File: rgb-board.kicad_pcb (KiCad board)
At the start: 2 copper layers, 178 x 129.5 mm, 89 parts, among them J1 Conn_02x25_Odd_Even, J10 Conn_Coaxial, J11 Conn_Coaxial, J2 SCART-F, J3 TEST_1P, J4 TEST_1P, J5 Conn_Coaxial, J6 Conn_Coaxial, J7 Conn_Coaxial, J8 Conn_Coaxial, J9 Conn_Coaxial, Q101 BC850C, Q105 BC850C, Q109 BC850C, Q113 BC850C, Q114 BC850C, Q201 BC850C, SW1 SW_DPDT_x2, U1 NCP1117-12_SOT223

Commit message: Update project to KiCad 8.
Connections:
- net /B/B-Y renamed /B/B-Y
- net /G/Y renamed /G/Y
- net /HD/CS renamed /HD/CS
- net /R/R-Y renamed /R/R-Y
- J1 pad 10: (no net) -> unconnected-(J1-Pin_10-Pad10)
- J1 pad 15: (no net) -> unconnected-(J1-Pin_15-Pad15)
- J1 pad 16: (no net) -> unconnected-(J1-Pin_16-Pad16)
- J1 pad 17: (no net) -> unconnected-(J1-Pin_17-Pad17)
- J1 pad 18: (no net) -> unconnected-(J1-Pin_18-Pad18)
- J1 pad 20: (no net) -> unconnected-(J1-Pin_20-Pad20)
- J1 pad 22: (no net) -> unconnected-(J1-Pin_22-Pad22)
- J1 pad 23: (no net) -> unconnected-(J1-Pin_23-Pad23)
- J1 pad 24: (no net) -> unconnected-(J1-Pin_24-Pad24)
- J1 pad 26: (no net) -> unconnected-(J1-Pin_26-Pad26)
- J1 pad 27: (no net) -> unconnected-(J1-Pin_27-Pad27)
- J1 pad 28: (no net) -> unconnected-(J1-Pin_28-Pad28)
- J1 pad 29: (no net) -> unconnected-(J1-Pin_29-Pad29)
- J1 pad 30: (no net) -> unconnected-(J1-Pin_30-Pad30)
- J1 pad 32: (no net) -> unconnected-(J1-Pin_32-Pad32)
- J1 pad 33: (no net) -> unconnected-(J1-Pin_33-Pad33)
- J1 pad 34: (no net) -> unconnected-(J1-Pin_34-Pad34)
- J1 pad 35: (no net) -> unconnected-(J1-Pin_35-Pad35)
- J1 pad 36: (no net) -> unconnected-(J1-Pin_36-Pad36)
- J1 pad 37: (no net) -> unconnected-(J1-Pin_37-Pad37)
- J1 pad 38: (no net) -> unconnected-(J1-Pin_38-Pad38)
- J1 pad 40: (no net) -> unconnected-(J1-Pin_40-Pad40)
- J1 pad 42: (no net) -> unconnected-(J1-Pin_42-Pad42)
- J1 pad 43: (no net) -> unconnected-(J1-Pin_43-Pad43)
- J1 pad 44: (no net) -> unconnected-(J1-Pin_44-Pad44)
- J1 pad 45: (no net) -> unconnected-(J1-Pin_45-Pad45)
- J1 pad 46: (no net) -> unconnected-(J1-Pin_46-Pad46)
- J1 pad 8: (no net) -> unconnected-(J1-Pin_8-Pad8)
- J1 pad 9: (no net) -> unconnected-(J1-Pin_9-Pad9)
- J2 pad 1: (no net) -> unconnected-(J2-P1-Pad1)
- J2 pad 10: (no net) -> unconnected-(J2-P10-Pad10)
- J2 pad 12: (no net) -> unconnected-(J2-P12-Pad12)
- J2 pad 14: (no net) -> unconnected-(J2-P14-Pad14)
- J2 pad 16: (no net) -> unconnected-(J2-P16-Pad16)
- J2 pad 19: (no net) -> unconnected-(J2-P19-Pad19)
- J2 pad 3: (no net) -> unconnected-(J2-P3-Pad3)
- J2 pad 8: (no net) -> unconnected-(J2-P8-Pad8)
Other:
- net class Default removed

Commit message: Remove BNC connectors.
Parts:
- removed J5, J6, J7, J8, J9: Conn_Coaxial, bnc-tht:BNC-THT

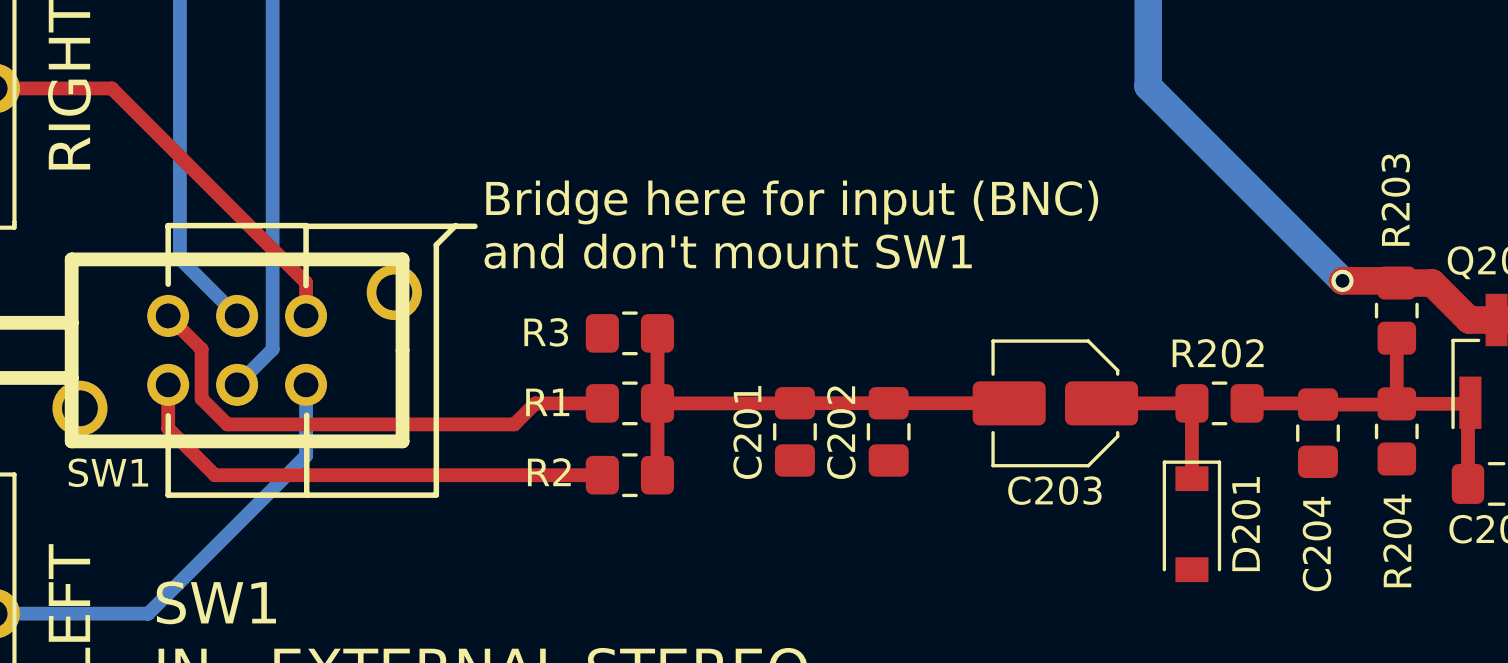
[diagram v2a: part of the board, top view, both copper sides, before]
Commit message: Remove BNC connectors.
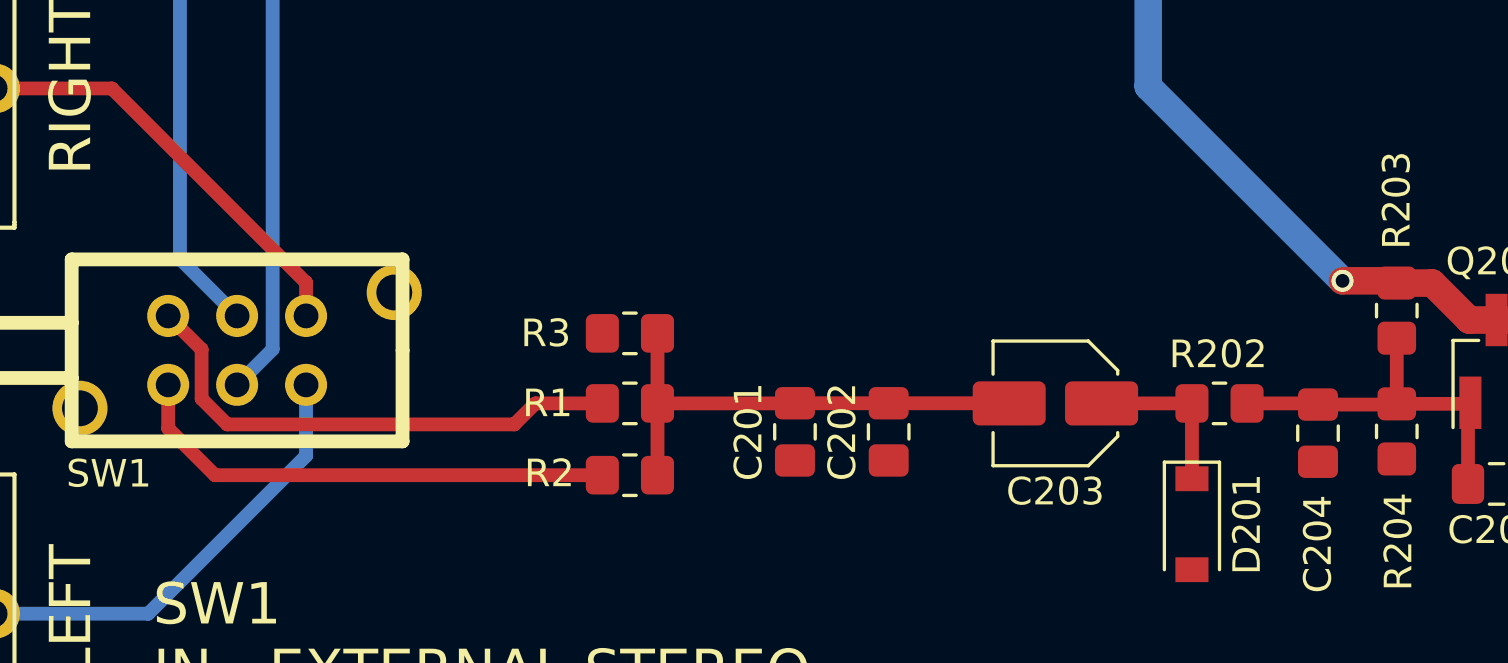
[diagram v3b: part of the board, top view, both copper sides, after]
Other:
- board text removed: "Bridge here for input (BNC) and don't mount SW1"
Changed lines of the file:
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@@
-	)
-	(gr_line
-		(start 65.55 137.6)
-		(end 65.55 135.525)
-		(stroke
-			(width 0.2)
-			(type solid)
-		)
-		(layer "F.SilkS")
 	)
 	(gr_line
@@
 	)
 	(gr_line
-		(start 70.575 142.35)
-		(end 70.575 145.25)
-		(stroke
-			(width 0.2)
-			(type solid)
-		)
-		(layer "F.SilkS")
-	)
-	(gr_line
-		(start 75.275 136.175)
-		(end 75.975 135.475)
-		(stroke
-			(width 0.2)
-			(type solid)
-		)
-		(layer "F.SilkS")
-	)
-	(gr_line
-		(start 65.55 135.475)
-		(end 65.55 135.525)
-		(stroke
-			(width 0.2)
-			(type solid)
-		)
-		(layer "F.SilkS")
-	)
-	(gr_line
 		(start 106.68 121.92)
 		(end 71.12 121.92)
@@
 	)
 	(gr_line
-		(start 70.55 135.475)
-		(end 65.55 135.475)
-		(stroke
-			(width 0.2)
-			(type solid)
-		)
-		(layer "F.SilkS")
-	)
-	(gr_line
-		(start 75.275 145.225)
-		(end 75.275 136.175)
-		(stroke
-			(width 0.2)
-			(type solid)
-		)
-		(layer "F.SilkS")
-	)
-	(gr_line
-		(start 65.55 142.375)
-		(end 65.55 145.25)
-		(stroke
-			(width 0.2)
-			(type solid)
-		)
-		(layer "F.SilkS")
-	)
-	(gr_line
-		(start 70.55 135.5)
-		(end 76.675 135.5)
-		(stroke
-			(width 0.2)
-			(type solid)
-		)
-		(layer "F.SilkS")
-	)
-	(gr_line
-		(start 70.55 137.65)
-		(end 70.55 135.475)
-		(stroke
-			(width 0.2)
-			(type solid)
-		)
-		(layer "F.SilkS")
-	)
-	(gr_line
 		(start 236.5 127.4)
 		(end 236.5 127.375)
@@
 	)
 	(gr_line
-		(start 65.55 145.25)
-		(end 75.275 145.25)
-		(stroke
-			(width 0.2)
-			(type solid)
-		)
-		(layer "F.SilkS")
-	)
-	(gr_line
 		(start 56.8 93.7)
 		(end 60.15 93.7)
@@
 		)
 	)
-	(gr_text "Bridge here for input (BNC)\nand don't mount SW1"
-		(at 76.925 135.5 0)
-		(layer "F.SilkS")
-		(effects
-			(font
-				(size 1.2 1.2)
-				(thickness 0.25)
-			)
-			(justify left)
-		)
-	)

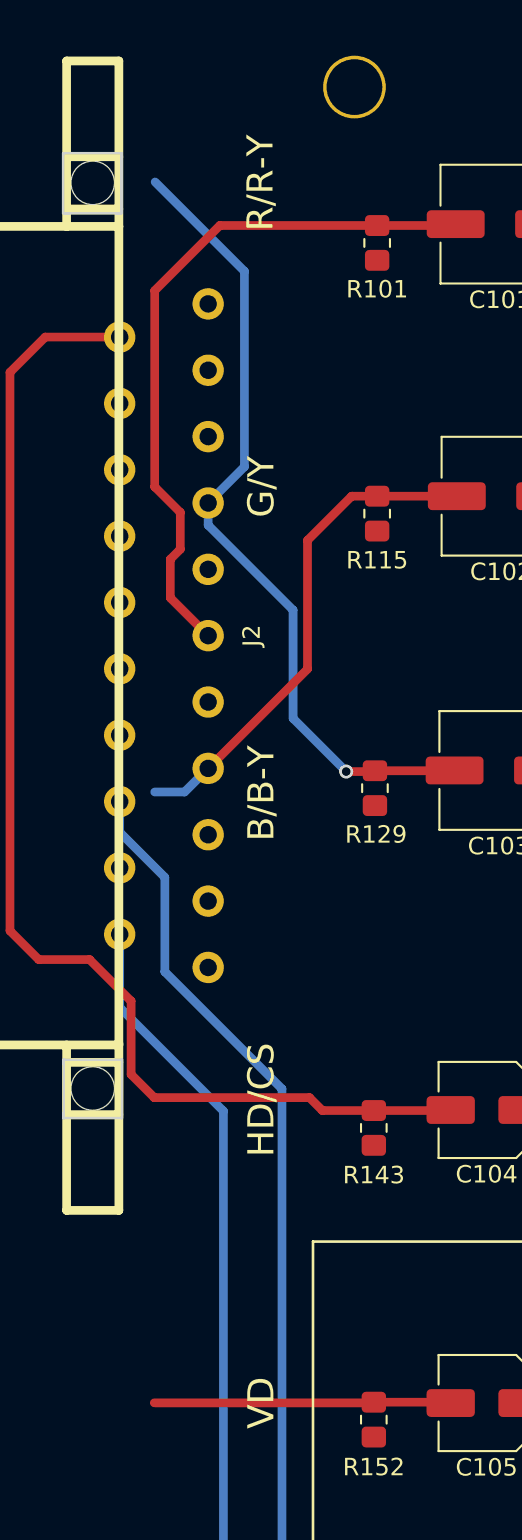
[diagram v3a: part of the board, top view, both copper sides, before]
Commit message: Remove BNC connectors.
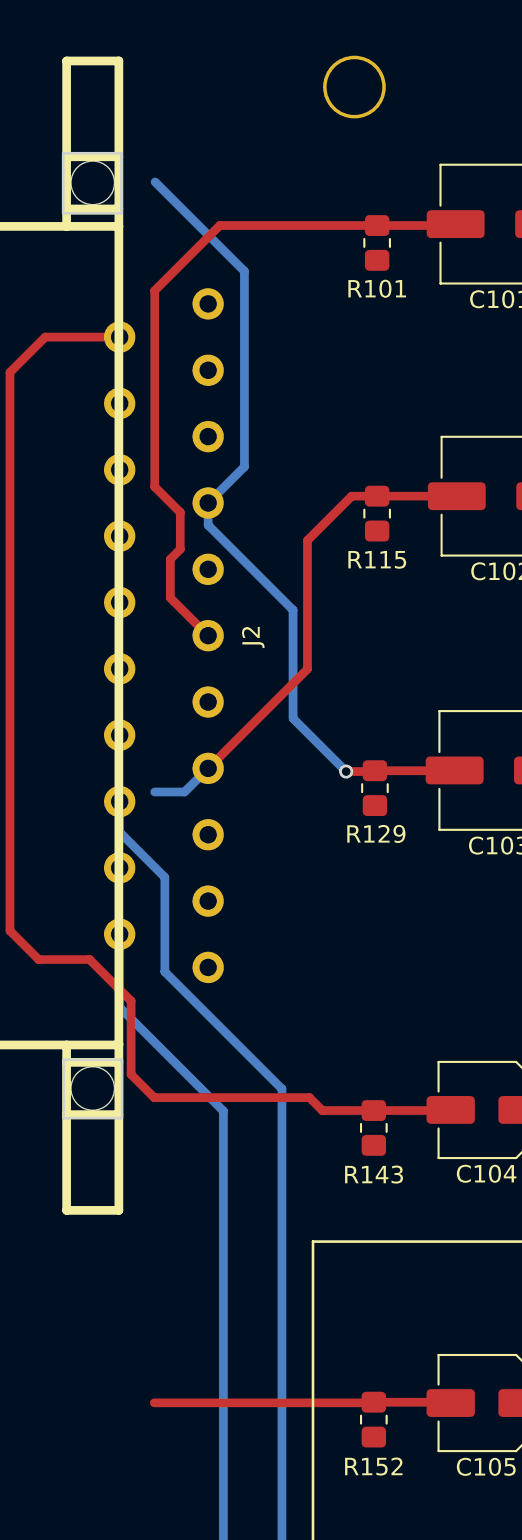
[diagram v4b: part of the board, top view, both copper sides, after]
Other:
- board text removed: "B/B-Y"
- board text removed: "G/Y"
- board text removed: "HD/CS"
- board text removed: "R/R-Y"
- board text removed: "VD"
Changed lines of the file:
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@@
-		)
-	)
-	(gr_text "VD"
-		(at 68.15 113.4 90)
-		(layer "F.SilkS")
-		(effects
-			(font
-				(size 1.5 1.5)
-				(thickness 0.3)
-			)
 		)
 	)
 	(gr_text "JVC IF-C01COMG (RGB/YPbPr) SCART/BNC SMD CLONE BOARD\n(2021) Martin Hejnfelt (martin@hejnfelt.com)\n\nDual input idea credit goes to James Vanderloeff!\n"
 		(at 182.45 39.675 0)
-		(layer "F.SilkS")
-		(effects
-			(font
-				(size 1.5 1.5)
-				(thickness 0.3)
-			)
-		)
-	)
-	(gr_text "R/R-Y"
-		(at 68.1 43.35 90)
 		(layer "F.SilkS")
 		(effects
@@
 		)
 	)
-	(gr_text "G/Y"
-		(at 68.15 60.8 90)
-		(layer "F.SilkS")
-		(effects
-			(font
-				(size 1.5 1.5)
-				(thickness 0.3)
-			)
-		)
-	)
-	(gr_text "B/B-Y"
-		(at 68.15 78.4 90)
-		(layer "F.SilkS")
-		(effects
-			(font
-				(size 1.5 1.5)
-				(thickness 0.3)
-			)
-		)
-	)
 	(gr_text "Do NOT mount\nthis section\nwhen using SCART"
 		(at 110.49 112.9665 90)
@@
 			)
 		)
-	)
-	(gr_text "HD/CS"
-		(at 68.15 96 90)
-		(layer "F.SilkS")
-		(effects
-			(font
-				(size 1.5 1.5)
-				(thickness 0.3)
-			)
-		)

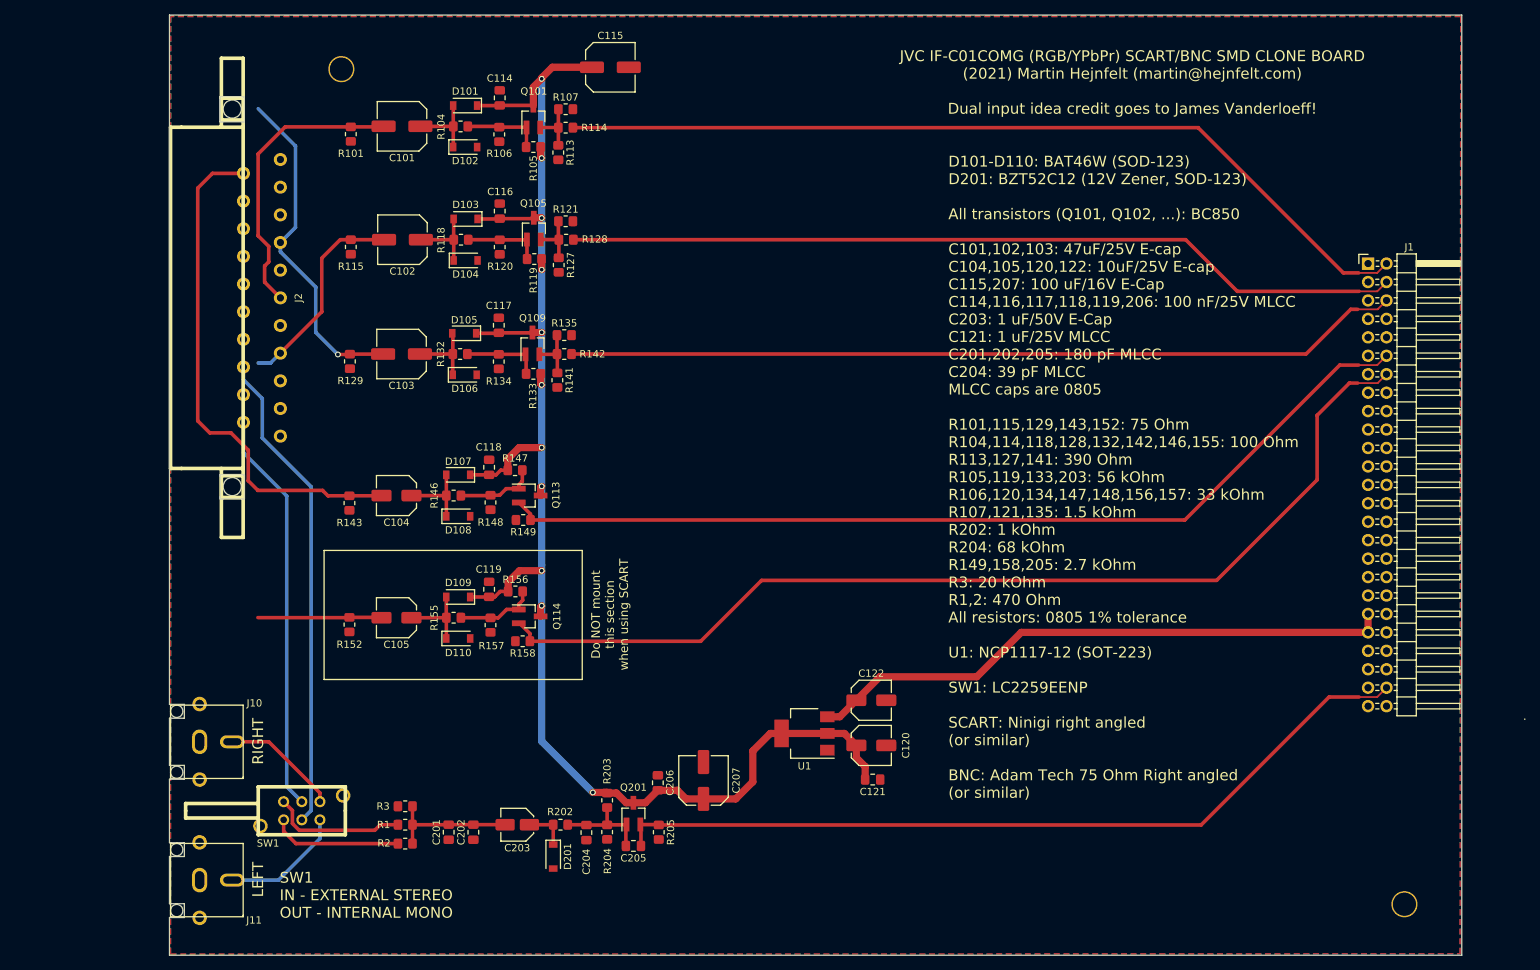
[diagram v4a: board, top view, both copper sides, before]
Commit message: Remove BNC connectors.
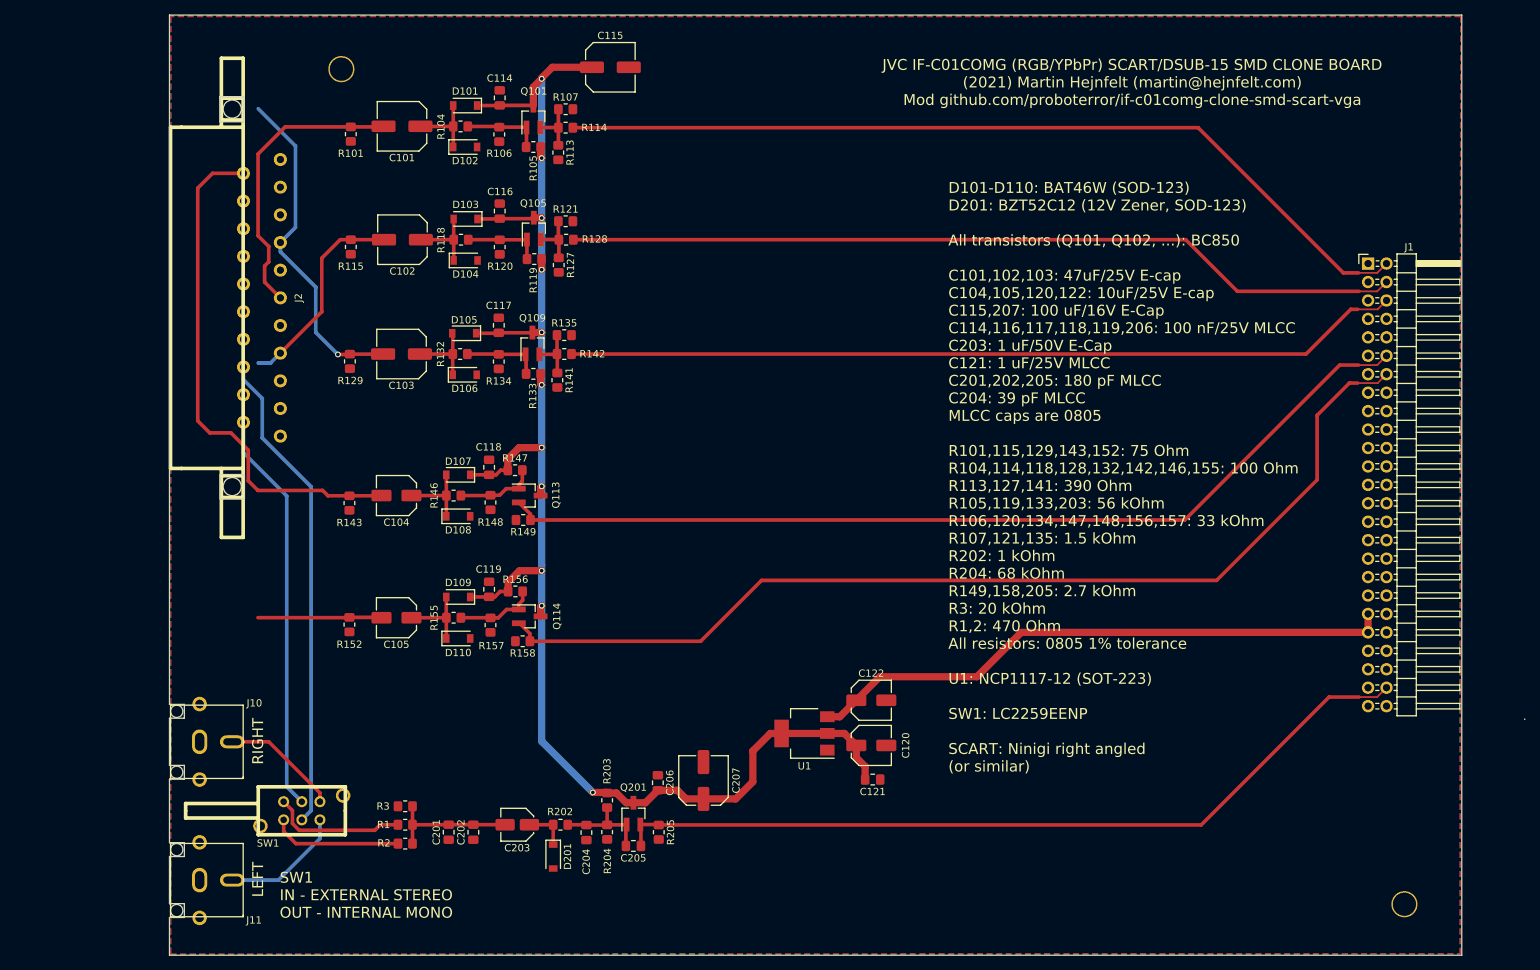
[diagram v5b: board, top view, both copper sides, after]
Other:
- board text added: "JVC IF-C01COMG (RGB/YPbPr) SCART/DSUB-15 SMD CLONE BOARD (2021) Martin Hejnfelt (martin@hejnfelt.com) Mod github.com/proboterror/if-c01comg-clone-smd-scart-vga"
- board text removed: "Do NOT mount this section when using SCART"
- board text removed: "JVC IF-C01COMG (RGB/YPbPr) SCART/BNC SMD CLONE BOARD (2021) Martin Hejnfelt (martin@hejnfelt.com) Dual input idea credit goes to James Vanderloeff!"
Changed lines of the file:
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@@
-	)
-	(gr_line
-		(start 71.12 121.92)
-		(end 71.12 104.14)
-		(stroke
-			(width 0.15)
-			(type solid)
-		)
-		(layer "F.SilkS")
-	)
-	(gr_line
-		(start 71.12 104.14)
-		(end 106.68 104.14)
-		(stroke
-			(width 0.15)
-			(type solid)
-		)
-		(layer "F.SilkS")
-	)
-	(gr_line
-		(start 106.68 104.14)
-		(end 106.68 121.92)
-		(stroke
-			(width 0.15)
-			(type solid)
-		)
-		(layer "F.SilkS")
-	)
-	(gr_line
-		(start 106.68 121.92)
-		(end 71.12 121.92)
-		(stroke
-			(width 0.15)
-			(type solid)
-		)
-		(layer "F.SilkS")
 	)
 	(gr_line
@@
 		(layer "Edge.Cuts")
 	)
-	(gr_text "D101-D110: BAT46W (SOD-123)\nD201: BZT52C12 (12V Zener, SOD-123)\n\nAll transistors (Q101, Q102, ...): BC850\n\nC101,102,103: 47uF/25V E-cap\nC104,105,120,122: 10uF/25V E-cap\nC115,207: 100 uF/16V E-Cap\nC114,116,117,118,119,206: 100 nF/25V MLCC\nC203: 1 uF/50V E-Cap\nC121: 1 uF/25V MLCC\nC201,202,205: 180 pF MLCC\nC204: 39 pF MLCC\nMLCC caps are 0805\n\nR101,115,129,143,152: 75 Ohm\nR104,114,118,128,132,142,146,155: 100 Ohm\nR113,127,141: 390 Ohm\nR105,119,133,203: 56 kOhm\nR106,120,134,147,148,156,157: 33 kOhm\nR107,121,135: 1.5 kOhm\nR202: 1 kOhm\nR204: 68 kOhm\nR149,158,205: 2.7 kOhm\nR3: 20 kOhm\nR1,2: 470 Ohm\nAll resistors: 0805 1% tolerance\n\nU1: NCP1117-12 (SOT-223)\n\nSW1: LC2259EENP\n\nSCART: Ninigi right angled\n(or similar)\n\nBNC: Adam Tech 75 Ohm Right angled\n(or similar)"
+	(gr_text "D101-D110: BAT46W (SOD-123)\nD201: BZT52C12 (12V Zener, SOD-123)\n\nAll transistors (Q101, Q102, ...): BC850\n\nC101,102,103: 47uF/25V E-cap\nC104,105,120,122: 10uF/25V E-cap\nC115,207: 100 uF/16V E-Cap\nC114,116,117,118,119,206: 100 nF/25V MLCC\nC203: 1 uF/50V E-Cap\nC121: 1 uF/25V MLCC\nC201,202,205: 180 pF MLCC\nC204: 39 pF MLCC\nMLCC caps are 0805\n\nR101,115,129,143,152: 75 Ohm\nR104,114,118,128,132,142,146,155: 100 Ohm\nR113,127,141: 390 Ohm\nR105,119,133,203: 56 kOhm\nR106,120,134,147,148,156,157: 33 kOhm\nR107,121,135: 1.5 kOhm\nR202: 1 kOhm\nR204: 68 kOhm\nR149,158,205: 2.7 kOhm\nR3: 20 kOhm\nR1,2: 470 Ohm\nAll resistors: 0805 1% tolerance\n\nU1: NCP1117-12 (SOT-223)\n\nSW1: LC2259EENP\n\nSCART: Ninigi right angled\n(or similar)"
 		(at 157.1 94.05 0)
 		(layer "F.SilkS")
@@
 		)
 	)
-	(gr_text "JVC IF-C01COMG (RGB/YPbPr) SCART/BNC SMD CLONE BOARD\n(2021) Martin Hejnfelt (martin@hejnfelt.com)\n\nDual input idea credit goes to James Vanderloeff!\n"
+	(gr_text "JVC IF-C01COMG (RGB/YPbPr) SCART/DSUB-15 SMD CLONE BOARD\n(2021) Martin Hejnfelt (martin@hejnfelt.com)\nMod github.com/proboterror/if-c01comg-clone-smd-scart-vga\n"
 		(at 182.45 39.675 0)
 		(layer "F.SilkS")
@@
 			)
 		)
-	)
-	(gr_text "Do NOT mount\nthis section\nwhen using SCART"
-		(at 110.49 112.9665 90)
-		(layer "F.SilkS")
-		(effects
-			(font
-				(size 1.2 1.2)
-				(thickness 0.25)
-			)
-		)
